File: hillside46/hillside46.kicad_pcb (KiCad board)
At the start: 2 copper layers, 142.5 x 99.9 mm, 92 parts, among them J1 I2C, J2 TRRS, J3 Bat_Pos, J4 Bat_Neg, J5 FFC2B28-12-G, K1 SW_Key, K10 SW_Key, K11 SW_Key, K12 SW_Key, K13 SW_Key, K14 SW_Key, K15 SW_Key, K16 SW_Key, K17 SW_Key, K18 SW_Key, K19 SW_Rotary, K2 SW_Key, K20 SW_Rotary, K21 SW_Key, K22 SW_Key, K23 SW_Key, K3 SW_Key, K4 SW_Key, K5 SW_Key, K6 SW_Key, K7 SW_Key, K8 SW_Key, K9 SW_Key, SW1 SKQGAFE010, SW2 SW_Power, U1 NiceNano2_r, U2 SRV05-4

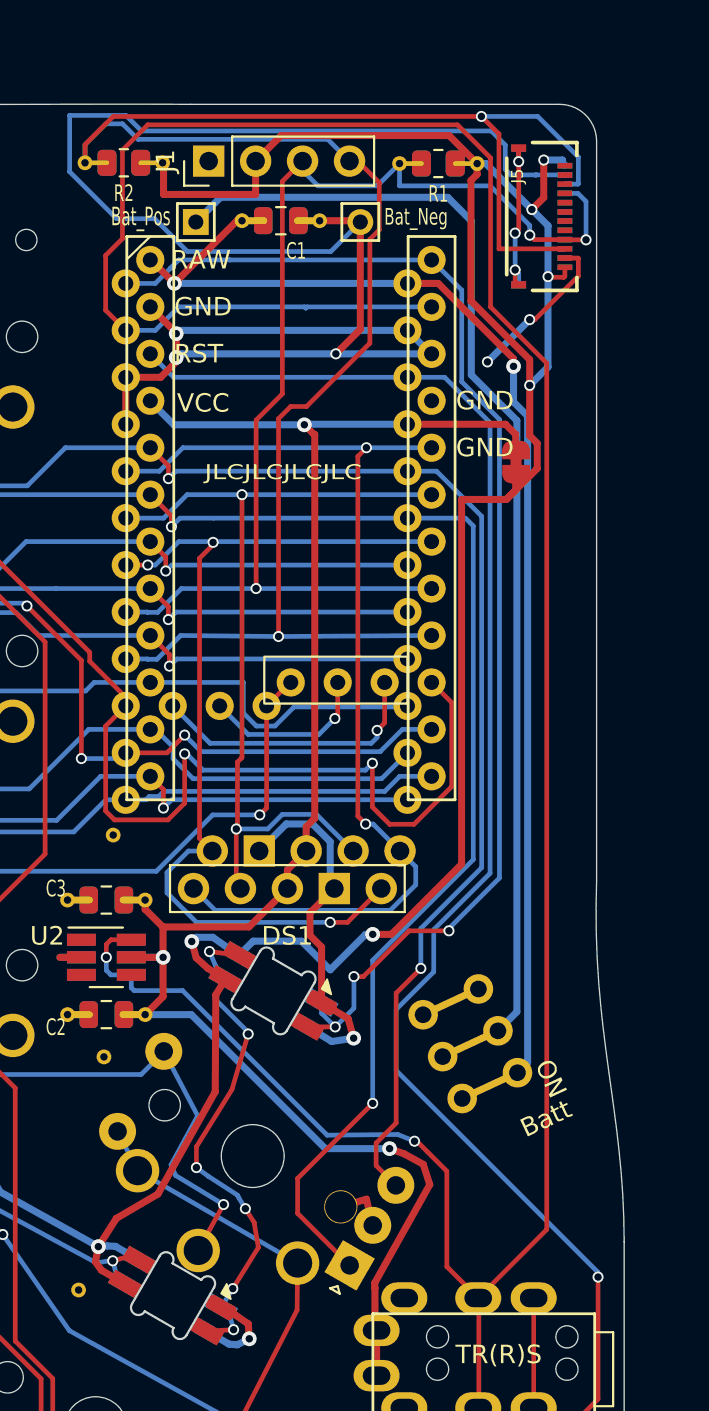
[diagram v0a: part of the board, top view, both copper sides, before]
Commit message: Updating FFC connector to use the same footprint as JLCPCB part and rotating by 180 degrees to orient correctly
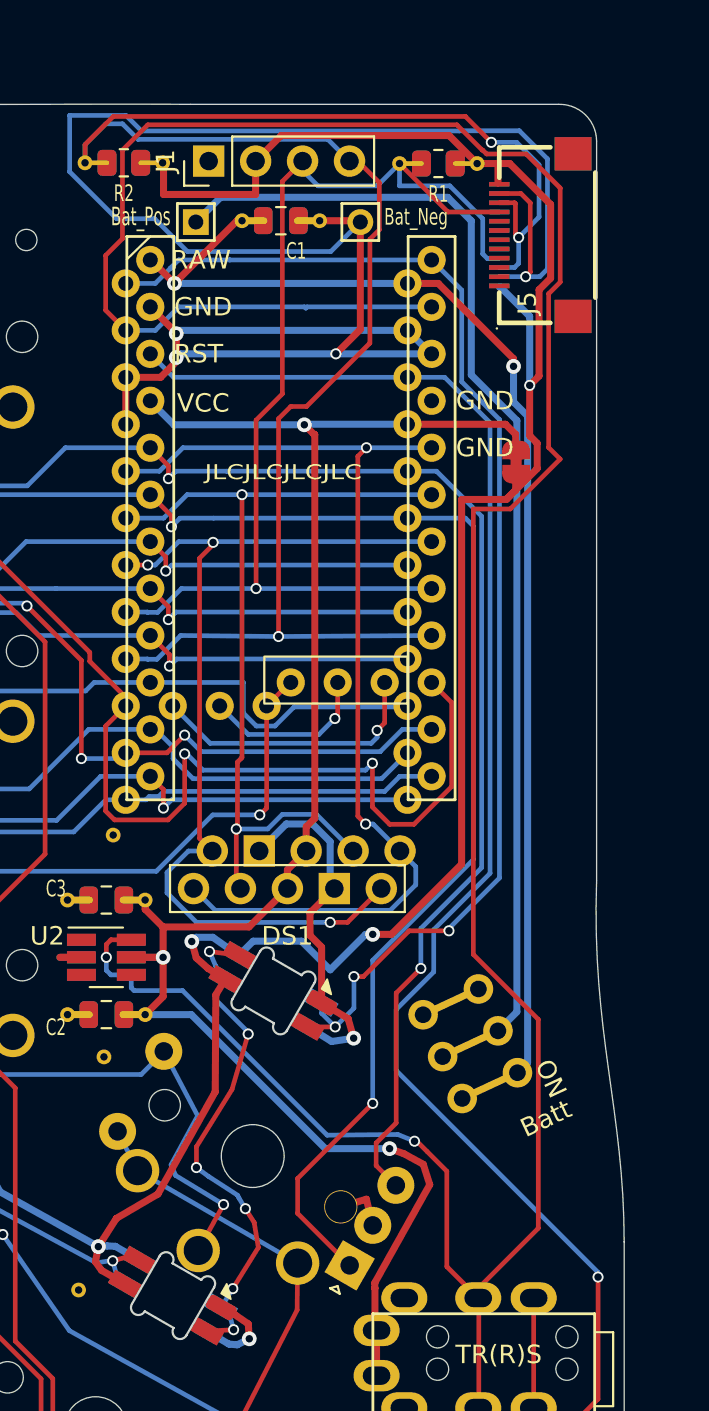
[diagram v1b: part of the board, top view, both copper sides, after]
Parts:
- J5: footprint FFC2B28-12-G:GCT_FFC2B28-12-G -> XF2M-1215-1A:FPC-SMD_12P-P0.50_XF2M-1215-1A
- moved J5 1.05 mm to (212.4, 51.7), turned to 90 degrees
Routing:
- net VCC_ACC: track 181.8 -> 170.6 mm, vias 9 -> 6
- net unconnected-(J5-PadS1): track 9.18 -> 0.00 mm, vias 3 -> 0
- net data: track 152.9 -> 159.6 mm
- net SDA: track 105.6 -> 100.1 mm, vias 2 -> 3
- net GND: track 148.2 -> 152.3 mm, vias 9 -> 8
- net SCL: track 64.1 -> 63.7 mm, vias 3 -> 1

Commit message: Updating pcb art
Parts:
- added G1: LOGO, wowee:wowee, B.Cu at (130.4, 110.2)
- J5: value FFC2B28-12-G -> XF2M-1215-1A
- moved H3 2.97 mm to (134.3, 105.1)
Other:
- board text removed: "Hillside View 46"

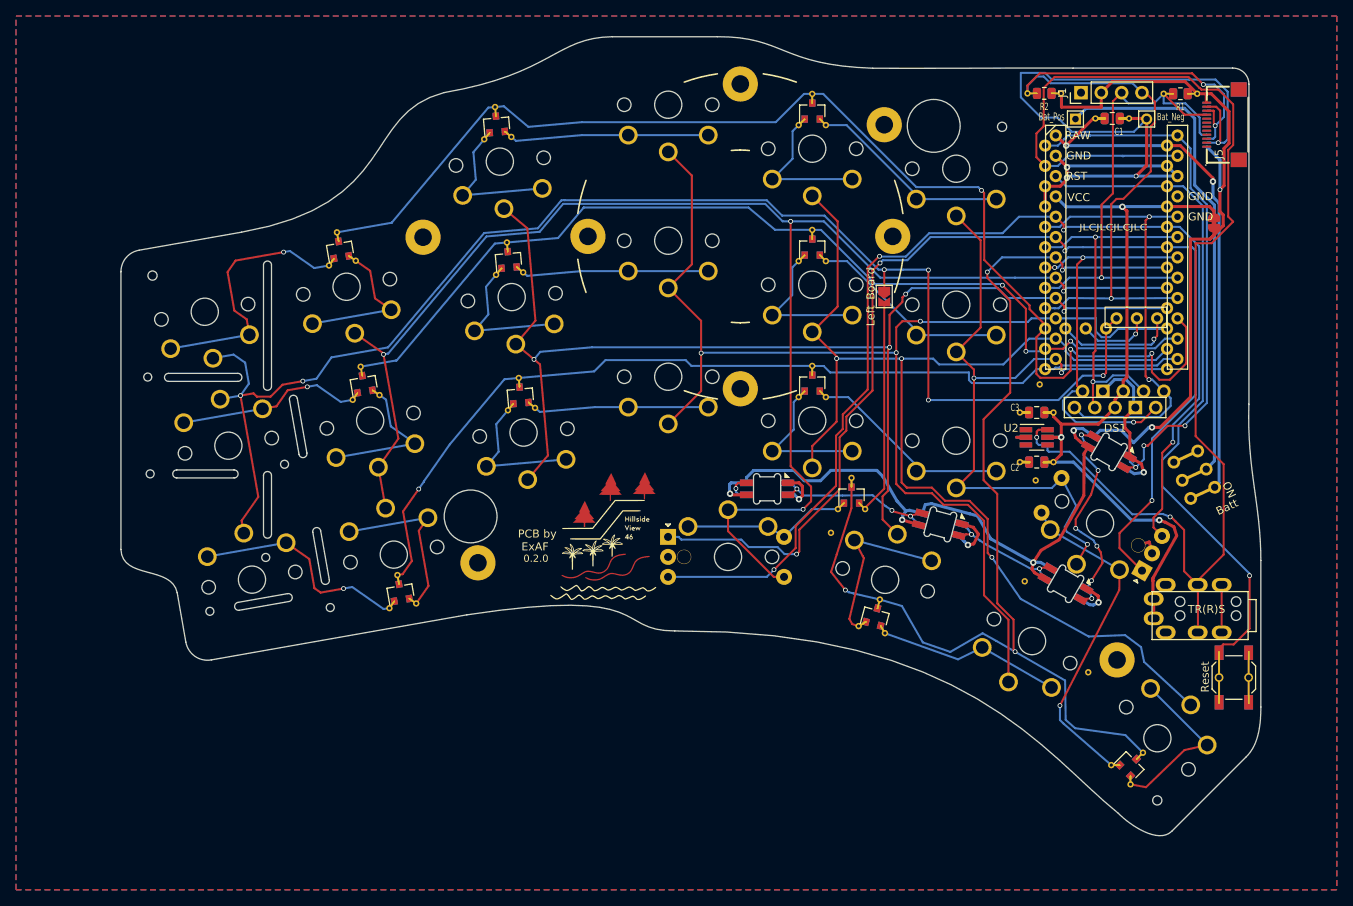
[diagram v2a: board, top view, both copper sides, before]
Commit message: Move switch, flip the copper on DS
Move the switch to the side of the PCB to make it easier to swtich.
Flip the copper layer for the display connector.
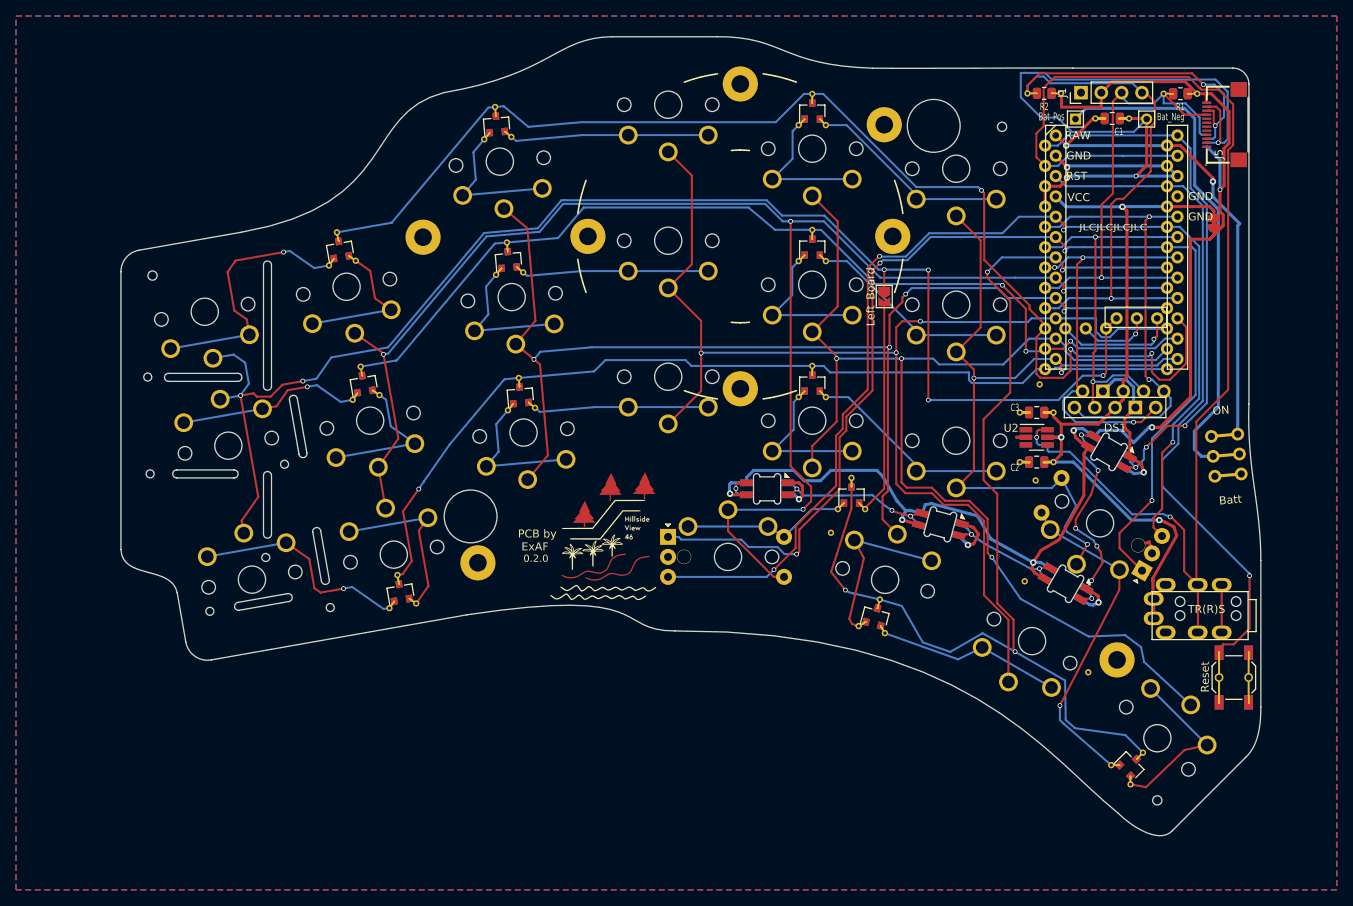
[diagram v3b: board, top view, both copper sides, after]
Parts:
- moved SW2 4.69 mm to (212.2, 93.0), turned to -85 degrees
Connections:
- SW2 pad 1: unconnected-(SW2-Pad1) -> raw
- SW2 pad 3: raw -> unconnected-(SW2-Pad3)
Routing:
- net raw: track 66.1 -> 60.4 mm
- net data: track 159.6 -> 154.5 mm
- net bat+: track 61.3 -> 62.5 mm
- net reset: track 85.0 -> 83.9 mm
- net Net-(D2-Pad2): track 16.2 -> 15.3 mm
- net Net-(D3-Pad2): track 21.4 -> 20.6 mm
- net Net-(D15-Pad2): track 15.6 -> 14.8 mm
- net Net-(D1-Pad2): track 27.8 -> 27.1 mm
- net Net-(D12-Pad2): track 15.5 -> 14.9 mm
- net Net-(D9-Pad2): track 15.4 -> 14.9 mm
- net SCL: track 63.7 -> 63.2 mm
